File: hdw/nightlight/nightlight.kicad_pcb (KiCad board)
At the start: 2 copper layers, 108 parts, among them J201 PICKIT3, J701 +12V IN AUX, J801 PIR Sensor, Q201 2N7002, Q601 BPW85A, Q701 IPC100N04S51R7ATMA1, Q702 IPC100N04S51R7ATMA1, SW201 MRST, SW401 Cap_Touch, U201 PIC16F1518-ISO, U301 LTC3624DD, U401 AT42QT1010-TSHR, U501 LT1618DD, U601 OPA340NA, U701 LTC4365DDB, U801 74LVC1G17, U901 74LVC1G06_Power, U902 74LVC1G06_Power, U903 74LVC1G06_Power, U904 74LVC1G06_Power, U905 74LVC1G06_Power

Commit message: Started arranging components on PCB
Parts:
- C601, C602, C603: moved to B.Cu
- moved U905 183.6 mm to (338.3, 15.4)
- moved D902 179.6 mm to (329.7, 11.1)
- moved R908 172.1 mm to (342.6, 14.7)
- moved U902 170.7 mm to (325.4, 10.5)
- moved D905 169.8 mm to (342.6, 16.4)
- moved C604 169.1 mm to (310.0, 57.2), turned to 180 degrees
- moved D903 168.6 mm to (330.2, 21.9)
- moved U903 168.4 mm to (325.8, 21.0)
- moved C902 164.3 mm to (325.4, 12.8), turned to 180 degrees
- moved R906 163.3 mm to (334.9, 16.3), turned to 270 degrees
- moved R903 163.1 mm to (329.6, 9.50)
- moved R602 162.8 mm to (310.0, 55.5), turned to 180 degrees
- moved C601 162.5 mm to (305.7, 56.2), turned to 180 degrees
- moved C603 161.4 mm to (305.7, 52.9), turned to 180 degrees
- moved C905 161.2 mm to (338.3, 17.9), turned to 180 degrees
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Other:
- copper layers 2 -> 4
- net class Power added: clearance 0.2, trace_width 0.635, via_dia 0.8, via_drill 0.4
- net class Signal added: clearance 0.2, trace_width 0.254, via_dia 0.8, via_drill 0.4

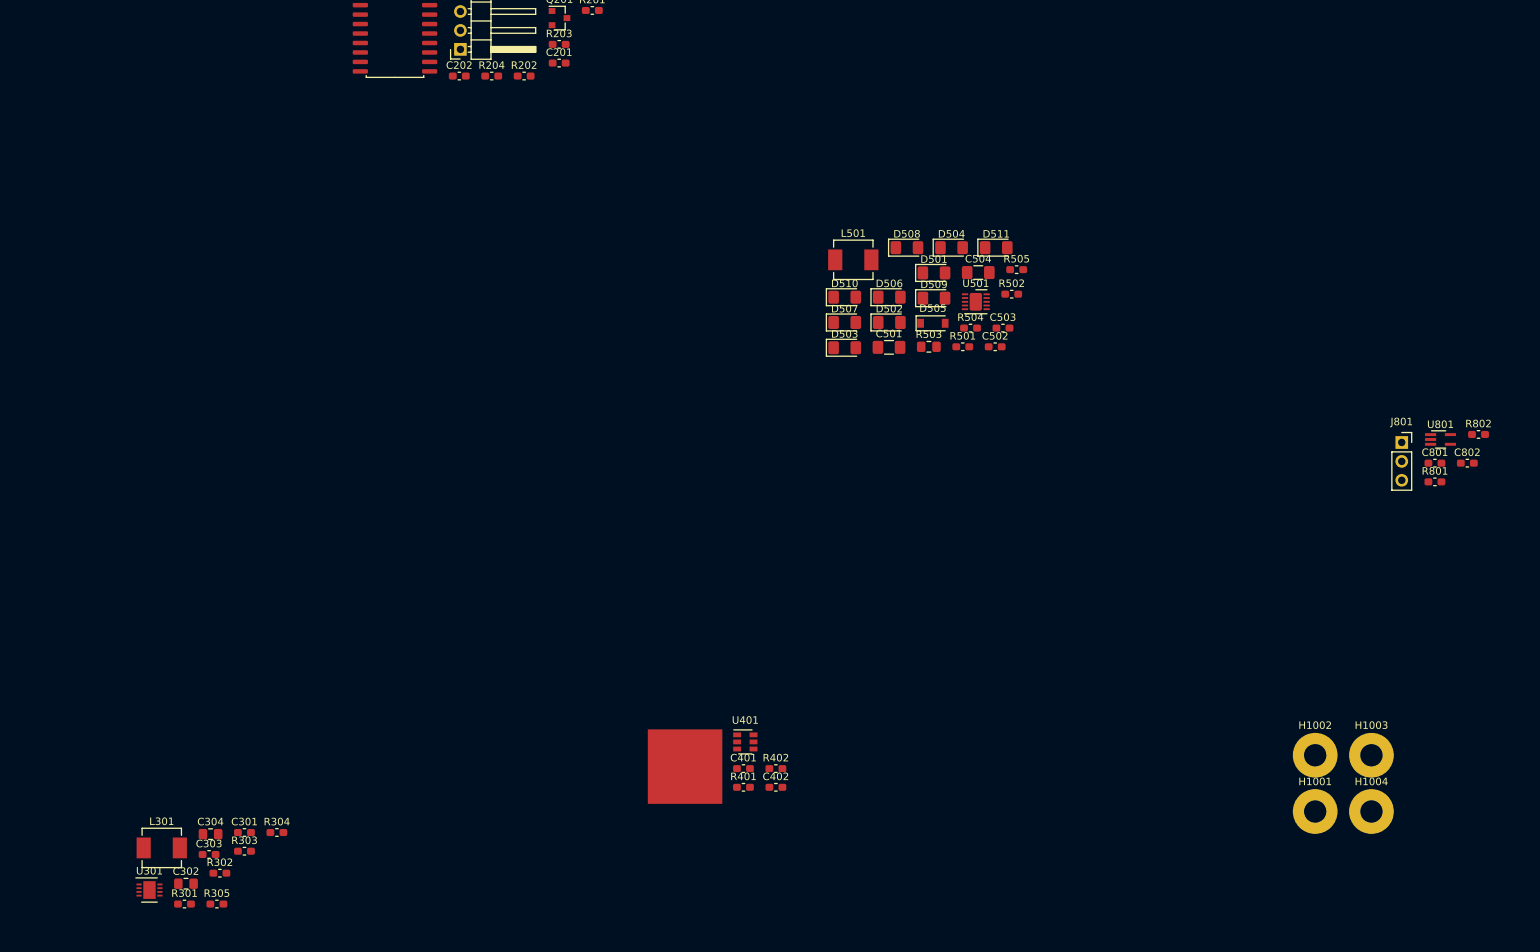
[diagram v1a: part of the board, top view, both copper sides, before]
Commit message: Arranged footprints for power button, buck converter
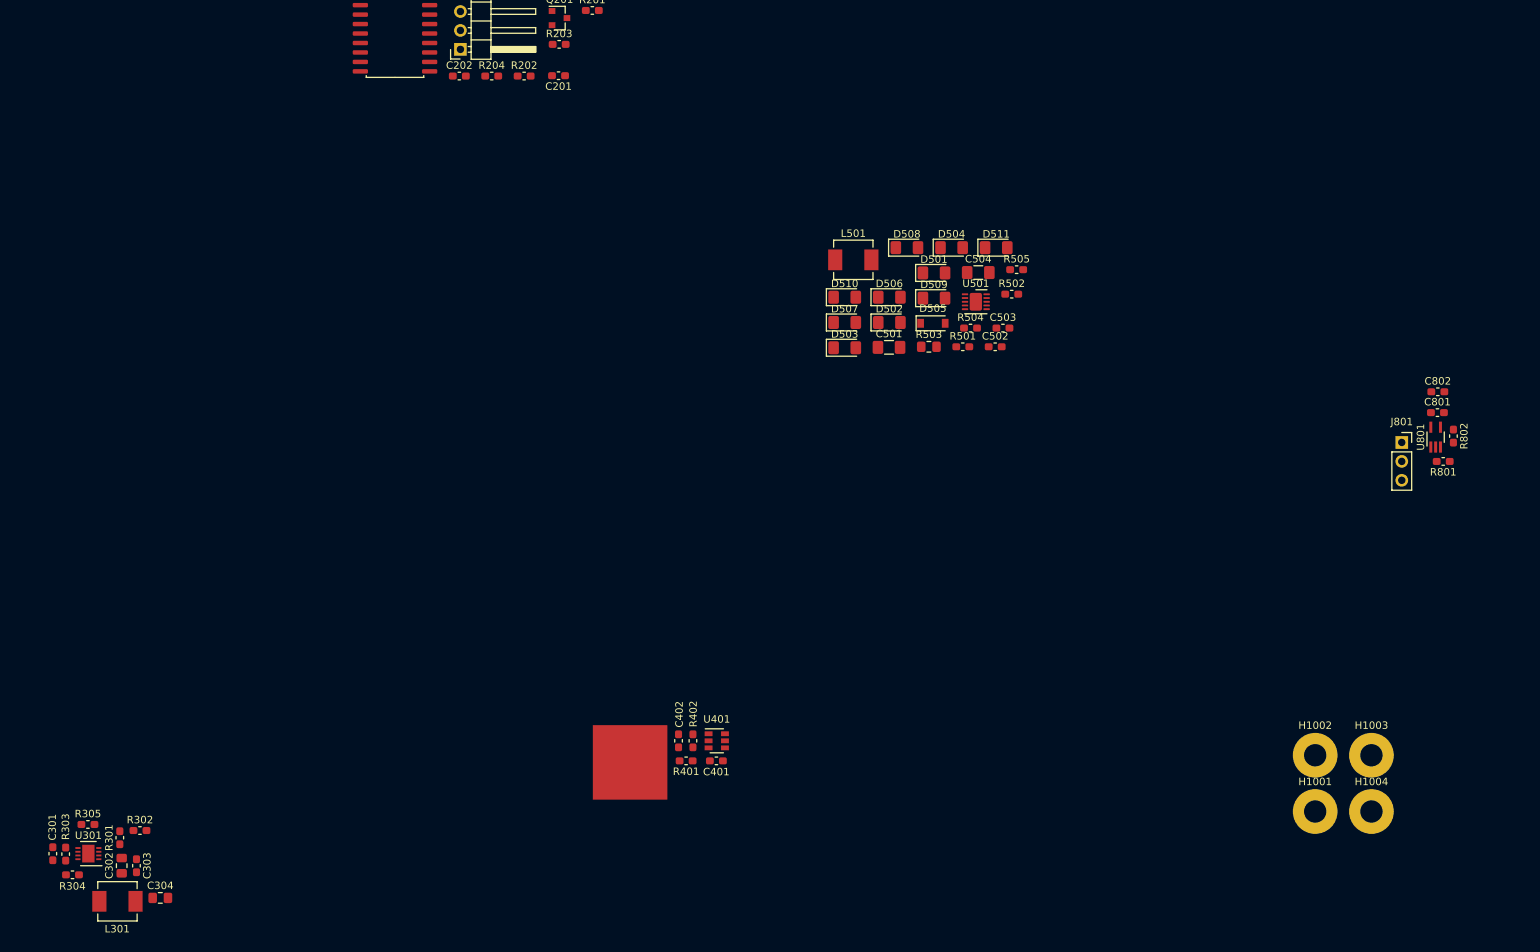
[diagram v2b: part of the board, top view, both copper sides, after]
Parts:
- moved R304 28.0 mm to (55.3, 143.5)
- moved C301 25.9 mm to (52.7, 140.6), turned to 270 degrees
- moved R303 24.0 mm to (54.4, 140.7), turned to 270 degrees
- moved R305 20.3 mm to (57.4, 136.7)
- moved C402 14.5 mm to (136.7, 125.5), turned to 270 degrees
- moved R301 12.4 mm to (61.7, 138.5), turned to 90 degrees
- moved R302 12.2 mm to (64.4, 137.5)
- moved R402 11.7 mm to (138.6, 125.5), turned to 270 degrees
- moved C304 10.9 mm to (67.1, 146.6)
- moved C802 10.4 mm to (238.5, 78.6)
- moved C303 9.86 mm to (63.9, 142.2), turned to 270 degrees
- moved U301 9.54 mm to (57.5, 140.6), turned to 180 degrees
- moved L301 9.31 mm to (61.4, 147.0)
- moved C302 8.96 mm to (61.9, 142.2), turned to 270 degrees
- moved R401 8.47 mm to (137.7, 128.2), turned to 180 degrees
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
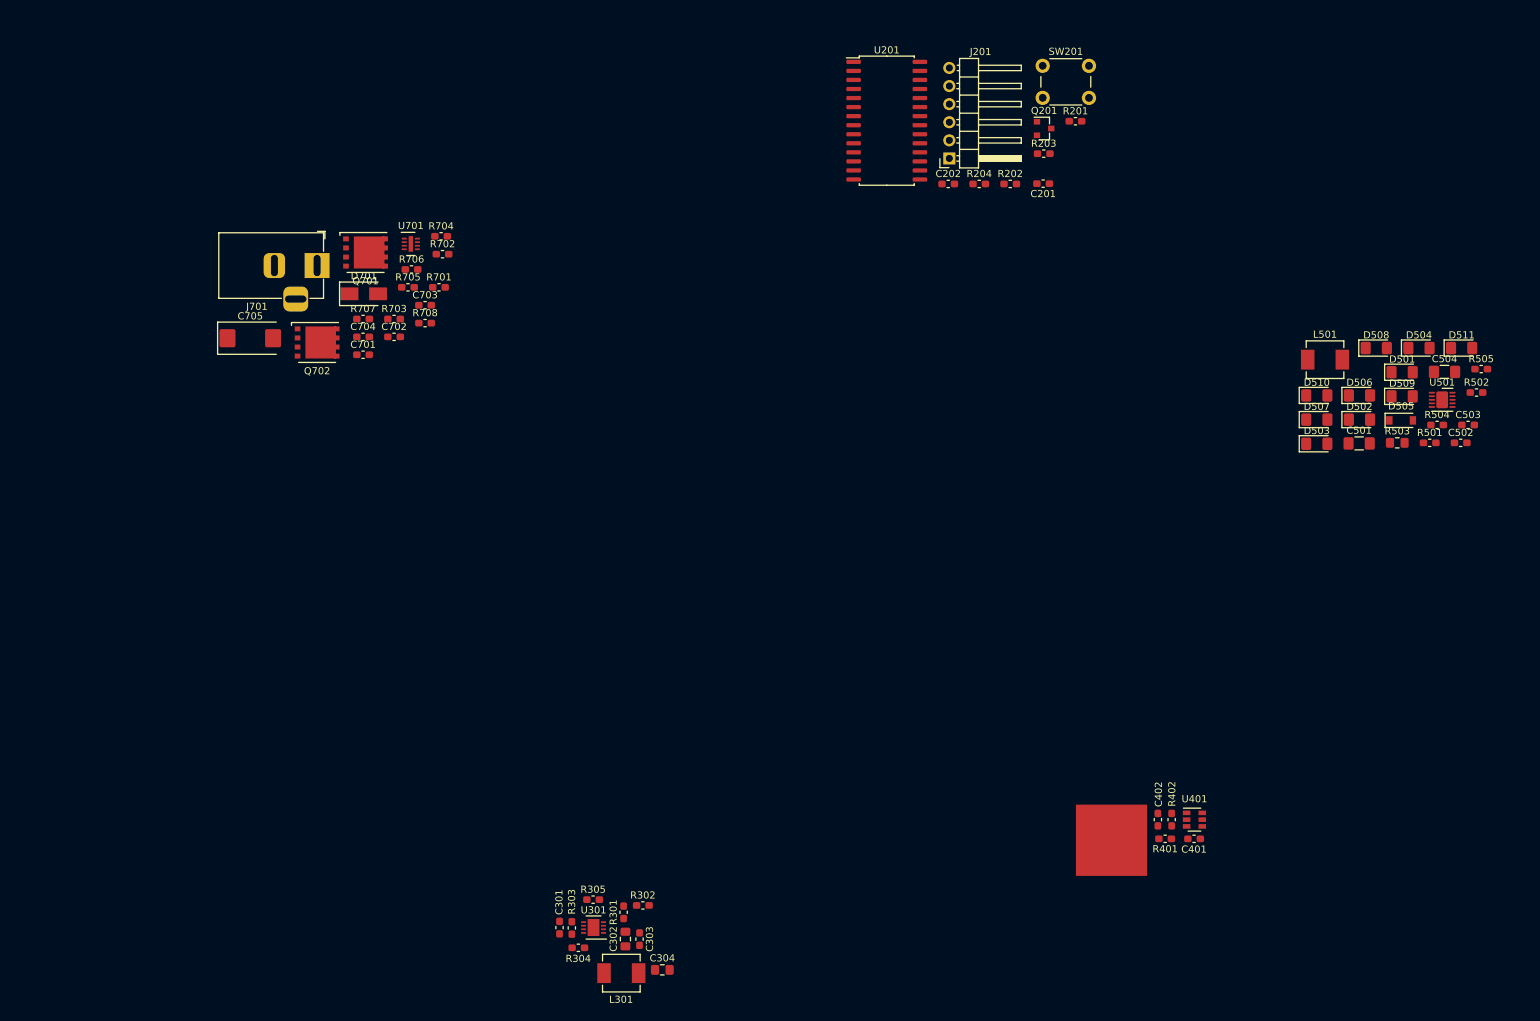
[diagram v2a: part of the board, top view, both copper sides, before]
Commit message: Finished arranging components on PCB
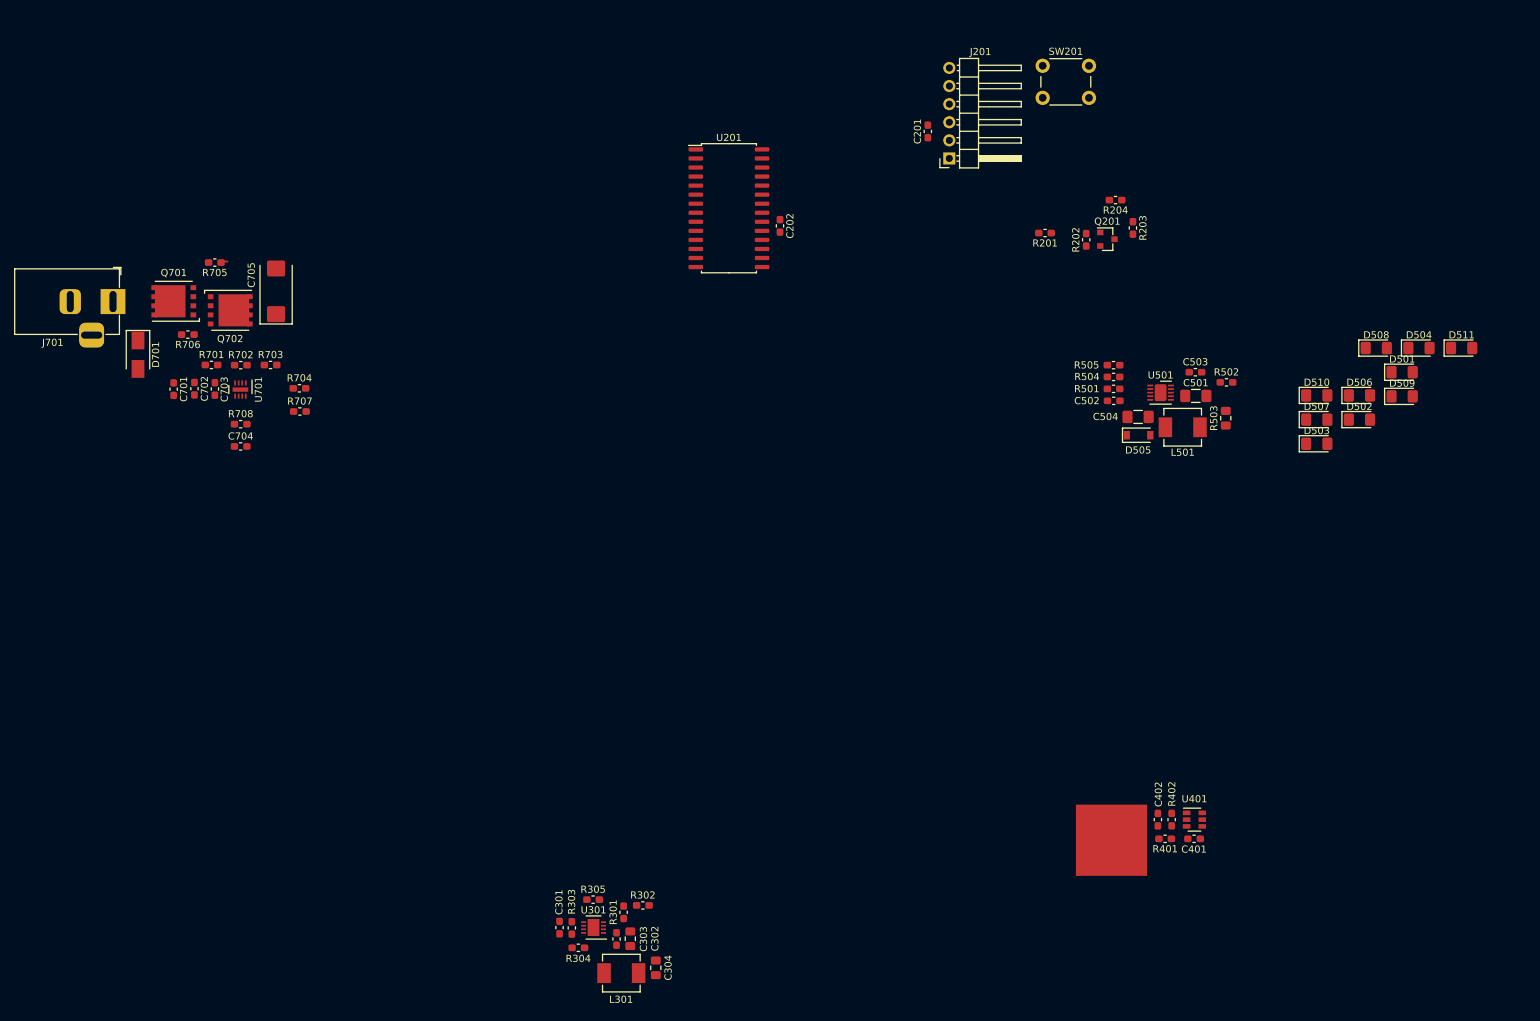
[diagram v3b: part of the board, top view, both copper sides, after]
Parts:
- moved R505 51.6 mm to (130.4, 61.7), turned to 180 degrees
- moved C502 49.0 mm to (130.5, 66.7), turned to 180 degrees
- moved R504 45.9 mm to (130.4, 63.3)
- moved R501 45.0 mm to (130.4, 65.0), turned to 180 degrees
- moved C504 43.5 mm to (133.9, 69.0)
- moved U501 39.5 mm to (137.0, 65.6)
- moved C503 39.0 mm to (141.9, 62.7)
- moved D505 36.9 mm to (133.9, 71.5)
- moved R502 35.1 mm to (146.3, 64.1)
- moved R701 33.7 mm to (3.84, 61.7)
- moved D701 32.8 mm to (-6.48, 60.2), turned to 270 degrees
- moved R706 32.7 mm to (0.52, 57.4), turned to 180 degrees
- moved R702 32.3 mm to (7.95, 61.7)
- moved C703 31.7 mm to (4.32, 65.0), turned to 270 degrees
- moved U701 31.5 mm to (7.90, 65.1), turned to 270 degrees
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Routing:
- net Net-(R705-Pad1): track 0.00 -> 0.62 mm

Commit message: Placed components on virtual board
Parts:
- added TP301: TP, Custom Footprints Library:Test_Point, B.Cu at (172.9, 75.8)
- added TP701: TP, Connector_PinHeader_2.54mm:PinHeader_1x01_P2.54mm_Horizontal, B.Cu at (96.9, 75.4)
- added TP702: TP, Custom Footprints Library:Test_Point, B.Cu at (172.2, 95.0)
- added TP703: TP, Custom Footprints Library:Test_Point, B.Cu at (153.5, 92.9)
- C201, C202, C301, C302, C303, C304, C401, C402, C501, C502, C503, C504, C604, C701, C702, C703, C704, C705, C801, C802, C901, C902, C903, C904, C905, D505, D701, D901, D902, D903, D904, D905, J201, L301, L501, Q201, Q701, Q702, R201, R202, R203, R204, R301, R302, R303, R304, R305, R401, R402, R501, R502, R503, R504, R505, R601, R602, R701, R702, R703, R704, R705, R706, R707, R708, R801, R802, R901, R902, R903, R904, R905, R906, R907, R908, SW201, U201, U301, U401, U501, U601, U701, U801, U901, U902, U903, U904, U905: moved to B.Cu
- moved D902 225.3 mm to (122.3, 99.0), turned to 90 degrees
- moved C902 224.6 mm to (120.1, 103.8), turned to 270 degrees
- moved R903 224.4 mm to (123.9, 99.1), turned to 90 degrees
- moved U902 223.4 mm to (122.4, 103.8), turned to 90 degrees
- moved R902 222.3 mm to (121.4, 107.1), turned to 180 degrees
- moved D904 217.4 mm to (113.2, 99.1), turned to 90 degrees
- moved R907 216.5 mm to (114.9, 99.1), turned to 90 degrees
- moved C904 216.0 mm to (111.5, 103.3), turned to 270 degrees
- moved U904 214.7 mm to (113.8, 103.4), turned to 90 degrees
- moved D903 214.5 mm to (130.0, 99.0), turned to 90 degrees
- moved R904 213.5 mm to (131.7, 99.1), turned to 90 degrees
- moved C903 213.2 mm to (128.5, 104.0), turned to 270 degrees
- moved D905 212.7 mm to (146.6, 98.9), turned to 90 degrees
- moved R905 212.3 mm to (115.2, 106.7), turned to 180 degrees
- moved U903 211.9 mm to (130.9, 104.0), turned to 90 degrees
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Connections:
- C801 pad 1: +3V3 -> +12V
- J801 pad 1: +3V3 -> +12V
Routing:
- net Net-(R705-Pad1): track 0.62 -> 0.00 mm
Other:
- board outline added: 100 x 50 mm
- board text added: "+12V"
- board text added: "+12V PGOOD"
- board text added: "+12Vin"
- board text added: "+3.3V"
- board text added: "+3.3V PGOOD"
- board text added: "GND"
- board text added: "analog error"
- board text added: "mnl_rst"
- board text added: "pir_out"
- board text added: "power"
- board text added: "reset"

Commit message: Started routing, minor schematic changes
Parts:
- moved C601 8.59 mm to (102.3, 84.6)
- moved C602 8.59 mm to (103.9, 84.6)
- moved C603 8.59 mm to (105.5, 84.6)
- moved SW201 8.26 mm to (94.9, 82.9), turned to 180 degrees
- moved C504 0.33 mm to (138.9, 116.5)
- moved C304 0.30 mm to (157.3, 79.6)
- moved R302 0.25 mm to (152.0, 89.6)
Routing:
- net +3V3: track 0.00 -> 33.2 mm, vias 0 -> 52
- net GND: track 0.00 -> 27.2 mm, vias 0 -> 44
- net Net-(R201-Pad2): track 0.00 -> 12.1 mm
- net reset: track 0.00 -> 10.9 mm
- net Net-(Q201-Pad1): track 0.00 -> 6.97 mm
- net Net-(R602-Pad2): track 0.00 -> 5.77 mm
- net Net-(L301-Pad1): track 0.00 -> 5.68 mm
- net +12Vin: track 0.00 -> 5.00 mm
- net Net-(D509-Pad2): track 0.00 -> 3.38 mm
- net Net-(D508-Pad2): track 0.00 -> 3.38 mm
- net Net-(D507-Pad2): track 0.00 -> 3.38 mm
- net Net-(D506-Pad2): track 0.00 -> 3.38 mm
- net Net-(D504-Pad2): track 0.00 -> 3.38 mm
- net Net-(D503-Pad2): track 0.00 -> 3.38 mm
- net Net-(D502-Pad2): track 0.00 -> 3.38 mm
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- added copper zone on B.Cu, net +12V
- added copper zone on B.Cu, net +12Vin
- added copper zone on B.Cu, net +3V3
- added copper zone on power.Cu, net +3V3
- added copper zone on B.Cu, net GND
- added copper zone on gnd.Cu, net GND
- added copper zone on B.Cu, net Net-(C504-Pad1)
- added copper zone on B.Cu, net Net-(D501-Pad1)
- added copper zone on B.Cu, net Net-(L301-Pad1)
- added copper zone on B.Cu, net Net-(Q701-Pad1)
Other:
- net class Default: clearance 0.2 -> 0.127; trace_width 0.25 -> 0.254; via_dia 0.8 -> 0.5588; via_drill 0.4 -> 0.199898
- net class Power: clearance 0.2 -> 0.127; via_dia 0.8 -> 0.5588; via_drill 0.4 -> 0.199898
- net class Signal: clearance 0.2 -> 0.127; via_dia 0.8 -> 0.5588; via_drill 0.4 -> 0.199898
- rule trace_clearance: 0.2 -> 0.127
- rule trace_min: 0.2 -> 0.0508
- rule via_min_drill: 0.3 -> 0.199898
- board text added: "Barrel Jack Polarity Layer Count Date JLC serial number location PICK KIT label cool art"

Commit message: finished PCD
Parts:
- added REF**: Symbol_Barrel_Polarity, Symbol:Symbol_Barrel_Polarity, F.Cu at (179.8, 95.7)
- J801: footprint Connector_PinSocket_2.54mm:PinSocket_1x03_P2.54mm_Vertical -> Custom Footprints Library:pirsensor
- moved C402 6.66 mm to (168.5, 119.0), turned to 90 degrees
- moved J801 1.35 mm to (132.7, 85.4), turned to 90 degrees
- moved R504 0.91 mm to (142.4, 110.3)
- moved R505 0.91 mm to (142.4, 108.6)
- turned R704 to 0 degrees
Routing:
- net Cap_Touch_Power: track 0.00 -> 86.7 mm
- net pir_out: track 0.00 -> 83.2 mm, vias 0 -> 4
- net +12V: track 2.03 -> 77.6 mm, vias 0 -> 3
- net +3V3: track 33.2 -> 107.5 mm, vias 52 -> 64
- net GND: track 27.2 -> 89.8 mm, vias 44 -> 61
- net led_pwm: track 0.00 -> 60.6 mm, vias 0 -> 2
- net led_enable: track 0.00 -> 46.2 mm, vias 0 -> 2
- net +12Vin: track 5.00 -> 49.7 mm
- net ~MCLR: track 0.00 -> 43.9 mm
- net Net-(D501-Pad1): track 0.00 -> 43.2 mm
- net POS3P3_PGOOD: track 0.00 -> 36.6 mm
- net Net-(R705-Pad1): track 0.00 -> 34.9 mm, vias 0 -> 3
- net POS12_PGOOD: track 0.00 -> 26.7 mm
- net light_level_adc: track 1.68 -> 28.1 mm, vias 0 -> 2
- net analog_error: track 2.03 -> 20.7 mm, vias 0 -> 2
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- added copper zone on B.Cu, net Net-(D505-Pad2)
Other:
- board text added: "+"
- board text added: "-"
- board text added: "12VIN"
- board text added: "JLCJLCJLCJLC"
- board text added: "PICKIT3"
- board text added: "nightlight 10/1/2019"
- board text removed: "Barrel Jack Polarity Layer Count Date JLC serial number location PICK KIT label cool art"
